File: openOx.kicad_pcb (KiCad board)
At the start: 2 copper layers, 89.3 x 53.4 mm, 43 parts, among them J1 SPI_1, J10 I2C_1, J11 Valve_3, J12 SR-04, J13 Valve_4, J14 O2_molex, J15 EXP1, J16 EXP2, J17 Analog_gnd, J18 Analog_in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

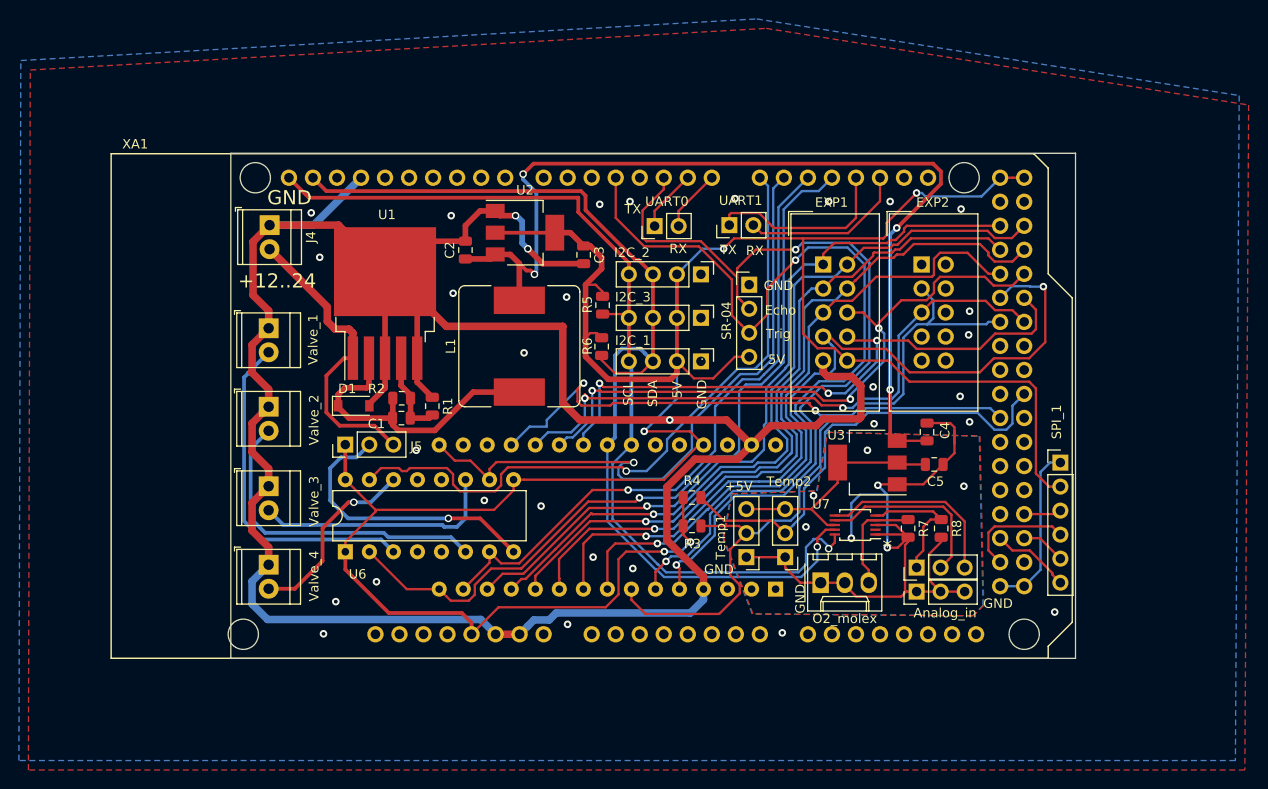
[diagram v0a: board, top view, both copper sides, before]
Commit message: outline changed, C2 package changed
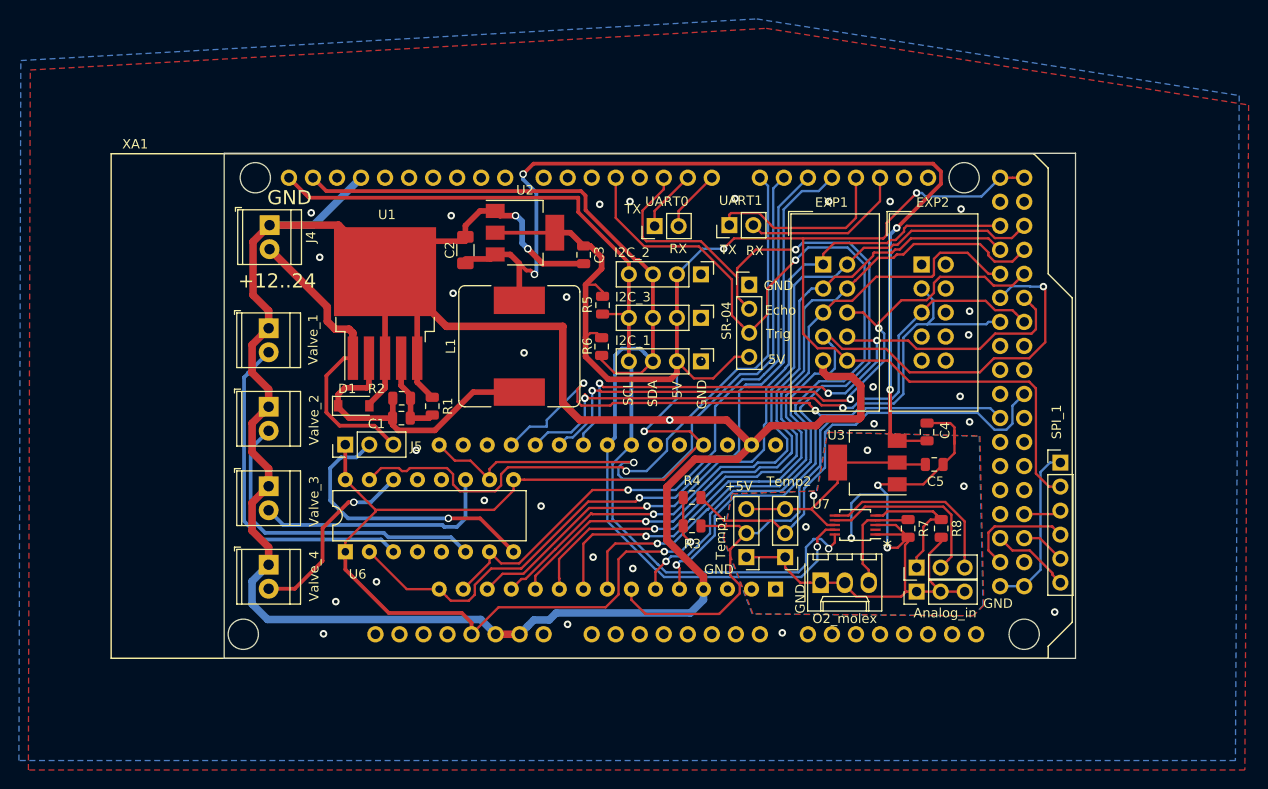
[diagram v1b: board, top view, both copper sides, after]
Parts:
- C2: footprint Capacitor_SMD:C_0805_2012Metric -> Capacitor_SMD:C_1206_3216Metric
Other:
- board size 89.3 x 53.4 mm -> 90 x 53.4 mm
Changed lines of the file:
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@@
     (thickness 1.6)
     (drawings 25)
-    (tracks 997)
+    (tracks 998)
     (zones 0)
     (modules 43)
@@
   (page A4)
   (layers
-    (0 F.Cu signal hide)
-    (31 B.Cu signal hide)
+    (0 F.Cu signal)
+    (31 B.Cu signal)
     (32 B.Adhes user)
     (33 F.Adhes user)
     (34 B.Paste user)
     (35 F.Paste user)
-    (36 B.SilkS user)
-    (37 F.SilkS user)
+    (36 B.SilkS user hide)
+    (37 F.SilkS user hide)
     (38 B.Mask user)
     (39 F.Mask user)
@@
   )
   (setup
-    (last_trace_width 0.25)
+    (last_trace_width 0.4)
     (user_trace_width 0.4)
     (user_trace_width 0.6)
@@
       (outputformat 1)
       (mirror false)
-      (drillshape 1)
+      (drillshape 0)
       (scaleselection 1)
-      (outputdirectory ""))
+      (outputdirectory "../../gerbers/inch/OpenOx"))
   )
   (net 0 "")
@@
     (add_net Valve4)
   )
+  (module Capacitor_SMD:C_1206_3216Metric (layer F.Cu)
+    (at 105 67.8375 90)
+    (descr "Capacitor SMD 1206 (3216 Metric), square (rectangular) end terminal, IPC_7351 nominal, (Body size source: http://www.tortai-tech.com/upload/download/2011102023233369053.pdf), generated with kicad-footprint-generator")
+    (tags capacitor)
+    (attr smd)
+    (fp_text reference C2 (at 0 -1.65 90) (layer F.SilkS)
+      (effects (font (size 1 1) (thickness 0.15)))
+    )
+    (fp_text value 100uF (at 0 1.65 90) (layer F.Fab)
+      (effects (font (size 1 1) (thickness 0.15)))
+    )
+    (fp_text user %R (at 0 0 90) (layer F.Fab)
+      (effects (font (size 0.5 0.5) (thickness 0.08)))
+    )
+    (fp_line (start 2.28 1.12) (end -2.28 1.12) (layer F.CrtYd) (width 0.05))
+    (fp_line (start 2.28 -1.12) (end 2.28 1.12) (layer F.CrtYd) (width 0.05))
+    (fp_line (start -2.28 -1.12) (end 2.28 -1.12) (layer F.CrtYd) (width 0.05))
+    (fp_line (start -2.28 1.12) (end -2.28 -1.12) (layer F.CrtYd) (width 0.05))
+    (fp_line (start -0.602064 0.91) (end 0.602064 0.91) (layer F.SilkS) (width 0.12))
+    (fp_line (start -0.602064 -0.91) (end 0.602064 -0.91) (layer F.SilkS) (width 0.12))
+    (fp_line (start 1.6 0.8) (end -1.6 0.8) (layer F.Fab) (width 0.1))
+    (fp_line (start 1.6 -0.8) (end 1.6 0.8) (layer F.Fab) (width 0.1))
+    (fp_line (start -1.6 -0.8) (end 1.6 -0.8) (layer F.Fab) (width 0.1))
+    (fp_line (start -1.6 0.8) (end -1.6 -0.8) (layer F.Fab) (width 0.1))
+    (pad 2 smd roundrect (at 1.4 0 90) (size 1.25 1.75) (layers F.Cu F.Paste F.Mask) (roundrect_rratio 0.2)
+      (net 5 GND))
+    (pad 1 smd roundrect (at -1.4 0 90) (size 1.25 1.75) (layers F.Cu F.Paste F.Mask) (roundrect_rratio 0.2)
+      (net 32 /7.5V))
+    (model ${KISYS3DMOD}/Capacitor_SMD.3dshapes/C_1206_3216Metric.wrl
+      (at (xyz 0 0 0))
+      (scale (xyz 1 1 1))
+      (rotate (xyz 0 0 0))
+    )
+  )
   (module Connector_IDC:IDC-Header_2x05_P2.54mm_Vertical (layer F.Cu)
     (at 142.82 69.36)
@@
   )
   (module Capacitor_SMD:C_0805_2012Metric (layer F.Cu)
-    (at 105 67.8375 90)
-    (descr "Capacitor SMD 0805 (2012 Metric), square (rectangular) end terminal, IPC_7351 nominal, (Body size source: https://docs.google.com/spreadsheets/d/1BsfQQcO9C6DZCsRaXUlFlo91Tg2WpOkGARC1WS5S8t0/edit?usp=sharing), generated with kicad-footprint-generator")
-    (tags capacitor)
-    (attr smd)
-    (fp_text reference C2 (at 0 -1.65 90) (layer F.SilkS)
-      (effects (font (size 1 1) (thickness 0.15)))
-    )
-    (fp_text value 100uF (at 0 1.65 90) (layer F.Fab)
-      (effects (font (size 1 1) (thickness 0.15)))
-    )
-    (fp_text user %R (at 0 0 90) (layer F.Fab)
-      (effects (font (size 0.5 0.5) (thickness 0.08)))
-    )
-    (fp_line (start 1.68 0.95) (end -1.68 0.95) (layer F.CrtYd) (width 0.05))
-    (fp_line (start 1.68 -0.95) (end 1.68 0.95) (layer F.CrtYd) (width 0.05))
-    (fp_line (start -1.68 -0.95) (end 1.68 -0.95) (layer F.CrtYd) (width 0.05))
-    (fp_line (start -1.68 0.95) (end -1.68 -0.95) (layer F.CrtYd) (width 0.05))
-    (fp_line (start -0.258578 0.71) (end 0.258578 0.71) (layer F.SilkS) (width 0.12))
-    (fp_line (start -0.258578 -0.71) (end 0.258578 -0.71) (layer F.SilkS) (width 0.12))
-    (fp_line (start 1 0.6) (end -1 0.6) (layer F.Fab) (width 0.1))
-    (fp_line (start 1 -0.6) (end 1 0.6) (layer F.Fab) (width 0.1))
-    (fp_line (start -1 -0.6) (end 1 -0.6) (layer F.Fab) (width 0.1))
-    (fp_line (start -1 0.6) (end -1 -0.6) (layer F.Fab) (width 0.1))
-    (pad 2 smd roundrect (at 0.9375 0 90) (size 0.975 1.4) (layers F.Cu F.Paste F.Mask) (roundrect_rratio 0.25)
-      (net 5 GND))
-    (pad 1 smd roundrect (at -0.9375 0 90) (size 0.975 1.4) (layers F.Cu F.Paste F.Mask) (roundrect_rratio 0.25)
-      (net 32 /7.5V))
-    (model ${KISYS3DMOD}/Capacitor_SMD.3dshapes/C_0805_2012Metric.wrl
-      (at (xyz 0 0 0))
-      (scale (xyz 1 1 1))
-      (rotate (xyz 0 0 0))
-    )
-  )
-  (module Capacitor_SMD:C_0805_2012Metric (layer F.Cu)
     (at 98.2375 85.6 180)
     (descr "Capacitor SMD 0805 (2012 Metric), square (rectangular) end terminal, IPC_7351 nominal, (Body size source: https://docs.google.com/spreadsheets/d/1BsfQQcO9C6DZCsRaXUlFlo91Tg2WpOkGARC1WS5S8t0/edit?usp=sharing), generated with kicad-footprint-generator")
@@
     (effects (font (size 1.5 1.5) (thickness 0.3)))
   )
-  (gr_line (start 80.2 111) (end 80.2 57.6) (layer Edge.Cuts) (width 0.05))
-  (gr_line (start 169.5 111) (end 80.2 111) (layer Edge.Cuts) (width 0.05))
+  (gr_line (start 79.5 111) (end 79.5 57.6) (layer Edge.Cuts) (width 0.05))
+  (gr_line (start 169.5 111) (end 79.5 111) (layer Edge.Cuts) (width 0.05))
   (gr_line (start 169.5 57.6) (end 169.5 111) (layer Edge.Cuts) (width 0.05))
-  (gr_line (start 80.2 57.6) (end 169.5 57.6) (layer Edge.Cuts) (width 0.05))
+  (gr_line (start 79.5 57.6) (end 169.5 57.6) (layer Edge.Cuts) (width 0.05))
   (segment (start 107.55 92.11) (end 105.54 90.1) (width 0.25) (layer F.Cu) (net 1))
   (segment (start 103.89 90.1) (end 102.23 88.44) (width 0.25) (layer F.Cu) (net 1))
@@
   (segment (start 148.7 75.534315) (end 151.095714 73.138601) (width 0.25) (layer F.Cu) (net 8))
   (segment (start 148.7 76.1) (end 148.7 75.534315) (width 0.25) (layer F.Cu) (net 8))
-  (segment (start 120.01 103.68) (end 120.01 99.69) (width 0.25) (layer F.Cu) (net 18))
-  (via (at 125.294282 98.858957) (size 0.8) (drill 0.4) (layers F.Cu B.Cu) (net 18))
-  (segment (start 120.01 99.69) (end 120.841043 98.858957) (width 0.25) (layer F.Cu) (net 18))
-  (segment (start 120.841043 98.858957) (end 125.294282 98.858957) (width 0.25) (layer F.Cu) (net 18))
-  (via (at 124.2 94.9) (size 0.8) (drill 0.4) (layers F.Cu B.Cu) (net 12))
   (segment (start 92.3 92.1) (end 92.31 92.11) (width 0.4) (layer F.Cu) (net 9))
   (segment (start 92.3 88.4) (end 92.3 92.1) (width 0.4) (layer F.Cu) (net 9))
@@
   (segment (start 148.1 68.45313) (end 148.1 68.2) (width 0.25) (layer F.Cu) (net 10))
   (segment (start 148.19998 68.10002) (end 150.1071 68.10002) (width 0.25) (layer F.Cu) (net 10))
+  (via (at 124.2 94.9) (size 0.8) (drill 0.4) (layers F.Cu B.Cu) (net 12))
   (segment (start 108.934979 102.055021) (end 107.31 103.68) (width 0.25) (layer F.Cu) (net 12))
   (segment (start 111.133643 102.055021) (end 108.934979 102.055021) (width 0.25) (layer F.Cu) (net 12))
@@
   (segment (start 123.594999 80.825001) (end 123.970001 80.449999) (width 0.25) (layer F.Cu) (net 17))
   (segment (start 119.4 78.975) (end 119.4 79.4625) (width 0.25) (layer F.Cu) (net 17))
+  (segment (start 120.01 103.68) (end 120.01 99.69) (width 0.25) (layer F.Cu) (net 18))
+  (via (at 125.294282 98.858957) (size 0.8) (drill 0.4) (layers F.Cu B.Cu) (net 18))
+  (segment (start 120.01 99.69) (end 120.841043 98.858957) (width 0.25) (layer F.Cu) (net 18))
+  (segment (start 120.841043 98.858957) (end 125.294282 98.858957) (width 0.25) (layer F.Cu) (net 18))
   (segment (start 143.683599 77.843599) (end 142.82 76.98) (width 0.25) (layer B.Cu) (net 18))
   (segment (start 144.058601 78.218601) (end 143.683599 77.843599) (width 0.25) (layer B.Cu) (net 18))
@@
   (segment (start 149.9 82.6) (end 149.9 87.25) (width 0.4) (layer F.Cu) (net 32))
   (segment (start 150.65 88) (end 153.8 88) (width 0.25) (layer F.Cu) (net 32))
+  (segment (start 105 69.2375) (end 105 68.775) (width 0.4) (layer F.Cu) (net 32))
   (segment (start 154.390001 103.090001) (end 155.24 103.94) (width 0.25) (layer F.Cu) (net 33))
   (segment (start 154.014999 102.714999) (end 154.390001 103.090001) (width 0.25) (layer F.Cu) (net 33))
